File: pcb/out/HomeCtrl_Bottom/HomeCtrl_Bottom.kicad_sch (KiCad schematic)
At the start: 24 parts, among them J1 12V IN, J2 UART, J3 B2B, SW1 EN, SW2 BOOT, U1 MP1584, U2 AMS1117-3.3, U3 ESP32-WROOM-32

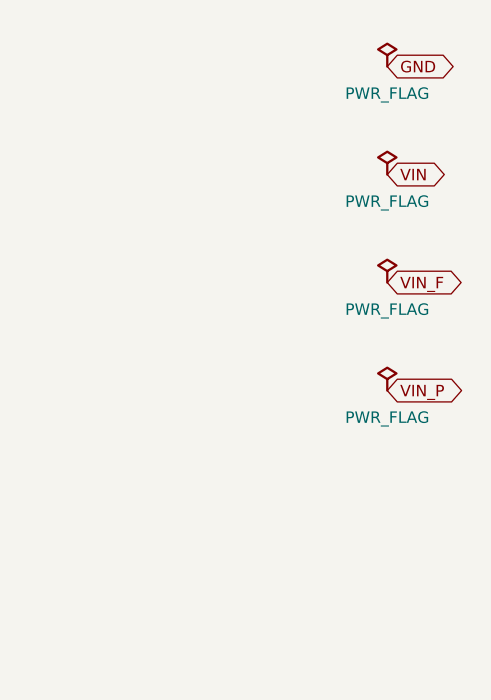
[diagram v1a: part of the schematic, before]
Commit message: HomeController PRO: sterownik domowy 32 wej / 16 wyj (2 plyty, 24V)
Nowe czesci: ESP32-C3 (modul kastelowany), TJA1051 (CAN), MOV (warystor),
MOSFET mocy DPAK (TO-252). Nowe bloki: wyjscie przekaznikowe 230V, wyjscie
MOSFET DC, bank wejsc RJ45 (TVS/wejscie), RS485, CAN, ESP32-C3, zlacze TFT.

Plyta DOLNA: 24V (bezpiecznik+dioda+MOV+buck5V+LDO3V3), ekspander wyjsc,
8x przekaznik 230V + 8x MOSFET DC, kazde wlasny zacisk; przekazniki we wnetrzu.
Plyta GORNA (wezsza): ESP32-C3 + 2x ekspander (32 wejscia), 8x RJ45, RS485+CAN,
TFT dotykowy. Otwory + B2B wspolne 1:1.

Layout: I/O na krawedzi dla OBU plyt (omija otwory narozne), zaciski 230V na
dolnej krawedzi, przekazniki we wnetrzu. Heurystyka zasilania rozpoznaje V24/Vxx;
regula diod tylko dla zlacz polowych (RJ45/zaciski). Niezawodnosc: TVS na kazdym
I/O, MOV, diody gasnace, pull-down bramek, grube sciezki 230V.

Oba PCB 0/0/0, zwalidowane kiutils (140 i 77 footprintow). Testy 12/12.

Co-Authored-By: Claude Opus 4.8 (1M context) <noreply@anthropic.com>
Claude-Session: https://claude.ai/code/session_01LNGxtK2Jv1rJLBLPTwFQ9C
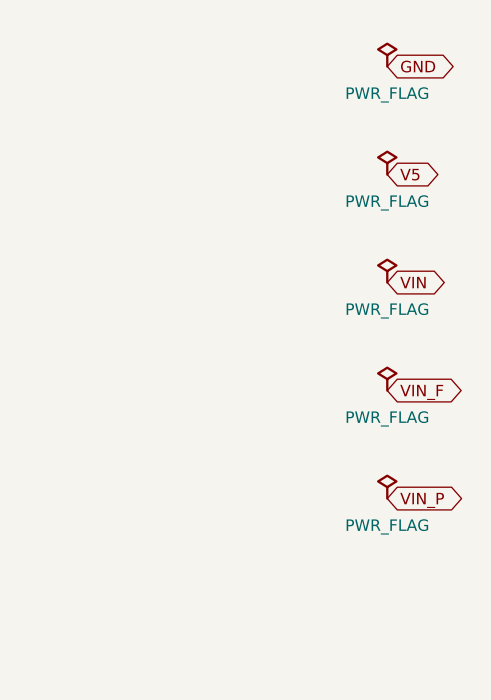
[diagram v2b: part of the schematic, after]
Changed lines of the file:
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@@
         "HomeCtrl_Bottom"
         (path
-          "/a5f34865-8952-4e0a-9267-8fb4a150fd35"
+          "/92ead28a-0ee8-4eed-82ee-55fd9d88155c"
           (reference "J1")
           (unit 1)
@@
         "HomeCtrl_Bottom"
         (path
-          "/a5f34865-8952-4e0a-9267-8fb4a150fd35"
+          "/92ead28a-0ee8-4eed-82ee-55fd9d88155c"
           (reference "F1")
           (unit 1)
@@
         "HomeCtrl_Bottom"
         (path
-          "/a5f34865-8952-4e0a-9267-8fb4a150fd35"
+          "/92ead28a-0ee8-4eed-82ee-55fd9d88155c"
           (reference "D1")
           (unit 1)
@@
         "HomeCtrl_Bottom"
         (path
-          "/a5f34865-8952-4e0a-9267-8fb4a150fd35"
+          "/92ead28a-0ee8-4eed-82ee-55fd9d88155c"
           (reference "C1")
           (unit 1)
@@
         "HomeCtrl_Bottom"
         (path
-          "/a5f34865-8952-4e0a-9267-8fb4a150fd35"
+          "/92ead28a-0ee8-4eed-82ee-55fd9d88155c"
           (reference "U1")
           (unit 1)
@@
         "HomeCtrl_Bottom"
         (path
-          "/a5f34865-8952-4e0a-9267-8fb4a150fd35"
+          "/92ead28a-0ee8-4eed-82ee-55fd9d88155c"
           (reference "L1")
           (unit 1)
@@
         "HomeCtrl_Bottom"
         (path
-          "/a5f34865-8952-4e0a-9267-8fb4a150fd35"
+          "/92ead28a-0ee8-4eed-82ee-55fd9d88155c"
           (reference "D2")
           (unit 1)
@@
         "HomeCtrl_Bottom"
         (path
-          "/a5f34865-8952-4e0a-9267-8fb4a150fd35"
+          "/92ead28a-0ee8-4eed-82ee-55fd9d88155c"
           (reference "C2")
           (unit 1)
@@
         "HomeCtrl_Bottom"
         (path
-          "/a5f34865-8952-4e0a-9267-8fb4a150fd35"
+          "/92ead28a-0ee8-4eed-82ee-55fd9d88155c"
           (reference "C3")
           (unit 1)
@@
         "HomeCtrl_Bottom"
         (path
-          "/a5f34865-8952-4e0a-9267-8fb4a150fd35"
+          "/92ead28a-0ee8-4eed-82ee-55fd9d88155c"
           (reference "R1")
           (unit 1)
@@
         "HomeCtrl_Bottom"
         (path
-          "/a5f34865-8952-4e0a-9267-8fb4a150fd35"
+          "/92ead28a-0ee8-4eed-82ee-55fd9d88155c"
           (reference "R2")
           (unit 1)
@@
         "HomeCtrl_Bottom"
         (path
-          "/a5f34865-8952-4e0a-9267-8fb4a150fd35"
+          "/92ead28a-0ee8-4eed-82ee-55fd9d88155c"
           (reference "U2")
           (unit 1)
@@
         "HomeCtrl_Bottom"
         (path
-          "/a5f34865-8952-4e0a-9267-8fb4a150fd35"
+          "/92ead28a-0ee8-4eed-82ee-55fd9d88155c"
           (reference "C5")
           (unit 1)
@@
         "HomeCtrl_Bottom"
         (path
-          "/a5f34865-8952-4e0a-9267-8fb4a150fd35"
+          "/92ead28a-0ee8-4eed-82ee-55fd9d88155c"
           (reference "C6")
           (unit 1)
@@
         "HomeCtrl_Bottom"
         (path
-          "/a5f34865-8952-4e0a-9267-8fb4a150fd35"
+          "/92ead28a-0ee8-4eed-82ee-55fd9d88155c"
           (reference "U3")
           (unit 1)
@@
         "HomeCtrl_Bottom"
         (path
-          "/a5f34865-8952-4e0a-9267-8fb4a150fd35"
+          "/92ead28a-0ee8-4eed-82ee-55fd9d88155c"
           (reference "C7")
           (unit 1)
@@
         "HomeCtrl_Bottom"
         (path
-          "/a5f34865-8952-4e0a-9267-8fb4a150fd35"
+          "/92ead28a-0ee8-4eed-82ee-55fd9d88155c"
           (reference "R3")
           (unit 1)
@@
         "HomeCtrl_Bottom"
         (path
-          "/a5f34865-8952-4e0a-9267-8fb4a150fd35"
+          "/92ead28a-0ee8-4eed-82ee-55fd9d88155c"
           (reference "C8")
           (unit 1)
@@
         "HomeCtrl_Bottom"
         (path
-          "/a5f34865-8952-4e0a-9267-8fb4a150fd35"
+          "/92ead28a-0ee8-4eed-82ee-55fd9d88155c"
           (reference "R4")
           (unit 1)
@@
         "HomeCtrl_Bottom"
         (path
-          "/a5f34865-8952-4e0a-9267-8fb4a150fd35"
+          "/92ead28a-0ee8-4eed-82ee-55fd9d88155c"
           (reference "R5")
           (unit 1)
@@
         "HomeCtrl_Bottom"
         (path
-          "/a5f34865-8952-4e0a-9267-8fb4a150fd35"
+          "/92ead28a-0ee8-4eed-82ee-55fd9d88155c"
           (reference "SW1")
           (unit 1)
@@
         "HomeCtrl_Bottom"
         (path
-          "/a5f34865-8952-4e0a-9267-8fb4a150fd35"
+          "/92ead28a-0ee8-4eed-82ee-55fd9d88155c"
           (reference "SW2")
           (unit 1)
@@
         "HomeCtrl_Bottom"
         (path
-          "/a5f34865-8952-4e0a-9267-8fb4a150fd35"
+          "/92ead28a-0ee8-4eed-82ee-55fd9d88155c"
           (reference "J2")
           (unit 1)
@@
         "HomeCtrl_Bottom"
         (path
-          "/a5f34865-8952-4e0a-9267-8fb4a150fd35"
+          "/92ead28a-0ee8-4eed-82ee-55fd9d88155c"
           (reference "J3")
           (unit 1)
@@
         "HomeCtrl_Bottom"
         (path
-          "/a5f34865-8952-4e0a-9267-8fb4a150fd35"
+          "/92ead28a-0ee8-4eed-82ee-55fd9d88155c"
           (reference "#FLG?")
           (unit 1)
@@
         "HomeCtrl_Bottom"
         (path
-          "/a5f34865-8952-4e0a-9267-8fb4a150fd35"
+          "/92ead28a-0ee8-4eed-82ee-55fd9d88155c"
           (reference "#FLG?")
           (unit 1)
@@
         "HomeCtrl_Bottom"
         (path
-          "/a5f34865-8952-4e0a-9267-8fb4a150fd35"
+          "/92ead28a-0ee8-4eed-82ee-55fd9d88155c"
           (reference "#FLG?")
           (unit 1)
@@
   )
   (global_label
-    "VIN"
+    "V5"
     (shape bidirectional)
     (at 250 49 0)
@@
         "HomeCtrl_Bottom"
         (path
-          "/a5f34865-8952-4e0a-9267-8fb4a150fd35"
+          "/92ead28a-0ee8-4eed-82ee-55fd9d88155c"
           (reference "#FLG?")
           (unit 1)
@@
   )
   (global_label
-    "VIN_F"
+    "VIN"
     (shape bidirectional)
     (at 250 61 0)
@@
         "HomeCtrl_Bottom"
         (path
-          "/a5f34865-8952-4e0a-9267-8fb4a150fd35"
+          "/92ead28a-0ee8-4eed-82ee-55fd9d88155c"
           (reference "#FLG?")
           (unit 1)
@@
   )
   (global_label
-    "VIN_P"
+    "VIN_F"
     (shape bidirectional)
     (at 250 73 0)
     (fields_autoplaced)
     (effects
+      (font
+        (size 1.27 1.27)
+      )
+    )
+  )
+  (symbol
+    (lib_id "pcbforge:PWR_FLAG")
+    (at 250 85 0)
+    (unit 1)
+    (exclude_from_sim no)
+    (in_bom no)
+    (on_board yes)
+    (dnp no)
+    (property
+      "Reference"
+      "#FLG?"
+      (at 250 82 0)
+      (effects
+        (font
+          (size 1.27 1.27)
+        )
+        (hide yes)
+      )
+    )
+    (property
+      "Value"
+      "PWR_FLAG"
+      (at 250 88 0)
+      (effects
+        (font
+          (size 1.27 1.27)
+        )
+      )
+    )
+    (property
+      "Footprint"
+      ""
+      (at 250 85 0)
+      (effects
+        (font
+          (size 1.27 1.27)
+        )
+        (hide yes)
+      )
+    )
+    (property
+      "Datasheet"
+      ""
+      (at 250 85 0)
+      (effects
+        (font
+          (size 1.27 1.27)
+        )
+        (hide yes)
+      )
+    )
+    (pin
+      "1"
+    )
+    (instances
+      (project
+        "HomeCtrl_Bottom"
+        (path
+          "/92ead28a-0ee8-4eed-82ee-55fd9d88155c"
+          (reference "#FLG?")
+          (unit 1)
+        )
+      )
+    )
+  )
+  (global_label
+    "VIN_P"
+    (shape bidirectional)
+    (at 250 85 0)
+    (fields_autoplaced)
+    (effects
